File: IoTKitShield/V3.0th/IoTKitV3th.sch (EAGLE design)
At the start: 28 parts, among them J1 4P-2.0, J2 4P-2.0, J3 4P-2.0, J4 4p-2.54

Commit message: Version fuer Produktion
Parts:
- renumbered SPI(V,G,SS,MO,MI,SLK) to SPI(V,G,D9,MO,MI,SLK)
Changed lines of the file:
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@@
 <part name="A2" library="pinhead" deviceset="PINHD-2X3" device=""/>
 <part name="A0" library="pinhead" deviceset="PINHD-2X3" device=""/>
-<part name="SPI(V,G,SS,MO,MI,SLK)" library="pinhead" deviceset="PINHD-1X6" device=""/>
+<part name="SPI(V,G,D9,MO,MI,SLK)" library="pinhead" deviceset="PINHD-1X6" device=""/>
 <part name="NFC/RFID" library="pinhead" deviceset="PINHD-1X8" device=""/>
 <part name="HALL-SENSOR" library="pinhead" deviceset="PINHD-1X3" device=""/>
@@
 <attribute name="VALUE" x="146.05" y="85.09" size="1.778" layer="96"/>
 </instance>
-<instance part="SPI(V,G,SS,MO,MI,SLK)" gate="A" x="11.43" y="127" rot="R90">
+<instance part="SPI(V,G,D9,MO,MI,SLK)" gate="A" x="11.43" y="127" rot="R90">
 <attribute name="NAME" x="0.635" y="120.65" size="1.778" layer="95" rot="R90"/>
 <attribute name="VALUE" x="21.59" y="120.65" size="1.778" layer="96" rot="R90"/>
@@
 </segment>
 <segment>
-<pinref part="SPI(V,G,SS,MO,MI,SLK)" gate="A" pin="3"/>
+<pinref part="SPI(V,G,D9,MO,MI,SLK)" gate="A" pin="3"/>
 <wire x1="8.89" y1="124.46" x2="8.89" y2="114.3" width="0.1524" layer="91"/>
 <label x="8.89" y="114.3" size="1.778" layer="95" rot="R90"/>
@@
 <wire x1="11.43" y1="124.46" x2="11.43" y2="114.3" width="0.1524" layer="91"/>
 <label x="11.43" y="114.3" size="1.778" layer="95" rot="R90"/>
-<pinref part="SPI(V,G,SS,MO,MI,SLK)" gate="A" pin="4"/>
+<pinref part="SPI(V,G,D9,MO,MI,SLK)" gate="A" pin="4"/>
 <junction x="11.43" y="124.46"/>
 </segment>
@@
 </segment>
 <segment>
-<pinref part="SPI(V,G,SS,MO,MI,SLK)" gate="A" pin="5"/>
+<pinref part="SPI(V,G,D9,MO,MI,SLK)" gate="A" pin="5"/>
 <wire x1="13.97" y1="124.46" x2="13.97" y2="114.3" width="0.1524" layer="91"/>
 <label x="13.97" y="114.3" size="1.778" layer="95" rot="R90"/>
@@
 </segment>
 <segment>
-<pinref part="SPI(V,G,SS,MO,MI,SLK)" gate="A" pin="6"/>
+<pinref part="SPI(V,G,D9,MO,MI,SLK)" gate="A" pin="6"/>
 <wire x1="16.51" y1="124.46" x2="16.51" y2="114.3" width="0.1524" layer="91"/>
 <label x="16.51" y="114.3" size="1.778" layer="95" rot="R90"/>
@@
 </segment>
 <segment>
-<pinref part="SPI(V,G,SS,MO,MI,SLK)" gate="A" pin="2"/>
+<pinref part="SPI(V,G,D9,MO,MI,SLK)" gate="A" pin="2"/>
 <pinref part="SUPPLY9" gate="+5V" pin="+5V"/>
 <wire x1="6.35" y1="124.46" x2="6.35" y2="118.364" width="0.1524" layer="91"/>
@@
 </segment>
 <segment>
-<pinref part="SPI(V,G,SS,MO,MI,SLK)" gate="A" pin="1"/>
+<pinref part="SPI(V,G,D9,MO,MI,SLK)" gate="A" pin="1"/>
 <pinref part="GND6" gate="1" pin="GND"/>
 <wire x1="3.81" y1="124.46" x2="3.81" y2="116.84" width="0.1524" layer="91"/>

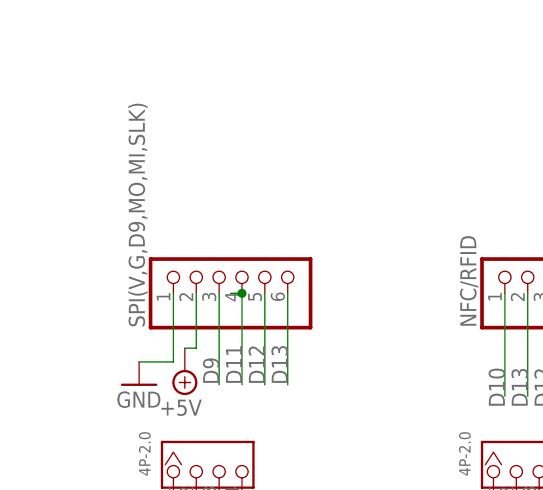
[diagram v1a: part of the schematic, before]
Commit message: Textkorrekturen
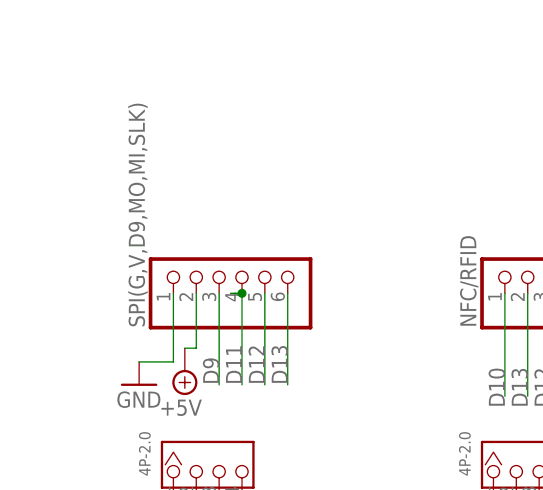
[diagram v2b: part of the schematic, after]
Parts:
- renumbered SPI(V,G,D9,MO,MI,SLK) to SPI(G,V,D9,MO,MI,SLK)
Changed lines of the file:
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@@
 <part name="A2" library="pinhead" deviceset="PINHD-2X3" device=""/>
 <part name="A0" library="pinhead" deviceset="PINHD-2X3" device=""/>
-<part name="SPI(V,G,D9,MO,MI,SLK)" library="pinhead" deviceset="PINHD-1X6" device=""/>
+<part name="SPI(G,V,D9,MO,MI,SLK)" library="pinhead" deviceset="PINHD-1X6" device=""/>
 <part name="NFC/RFID" library="pinhead" deviceset="PINHD-1X8" device=""/>
 <part name="HALL-SENSOR" library="pinhead" deviceset="PINHD-1X3" device=""/>
@@
 <attribute name="VALUE" x="146.05" y="85.09" size="1.778" layer="96"/>
 </instance>
-<instance part="SPI(V,G,D9,MO,MI,SLK)" gate="A" x="11.43" y="127" rot="R90">
+<instance part="SPI(G,V,D9,MO,MI,SLK)" gate="A" x="11.43" y="127" rot="R90">
 <attribute name="NAME" x="0.635" y="120.65" size="1.778" layer="95" rot="R90"/>
 <attribute name="VALUE" x="21.59" y="120.65" size="1.778" layer="96" rot="R90"/>
@@
 </segment>
 <segment>
-<pinref part="SPI(V,G,D9,MO,MI,SLK)" gate="A" pin="3"/>
+<pinref part="SPI(G,V,D9,MO,MI,SLK)" gate="A" pin="3"/>
 <wire x1="8.89" y1="124.46" x2="8.89" y2="114.3" width="0.1524" layer="91"/>
 <label x="8.89" y="114.3" size="1.778" layer="95" rot="R90"/>
@@
 <wire x1="11.43" y1="124.46" x2="11.43" y2="114.3" width="0.1524" layer="91"/>
 <label x="11.43" y="114.3" size="1.778" layer="95" rot="R90"/>
-<pinref part="SPI(V,G,D9,MO,MI,SLK)" gate="A" pin="4"/>
+<pinref part="SPI(G,V,D9,MO,MI,SLK)" gate="A" pin="4"/>
 <junction x="11.43" y="124.46"/>
 </segment>
@@
 </segment>
 <segment>
-<pinref part="SPI(V,G,D9,MO,MI,SLK)" gate="A" pin="5"/>
+<pinref part="SPI(G,V,D9,MO,MI,SLK)" gate="A" pin="5"/>
 <wire x1="13.97" y1="124.46" x2="13.97" y2="114.3" width="0.1524" layer="91"/>
 <label x="13.97" y="114.3" size="1.778" layer="95" rot="R90"/>
@@
 </segment>
 <segment>
-<pinref part="SPI(V,G,D9,MO,MI,SLK)" gate="A" pin="6"/>
+<pinref part="SPI(G,V,D9,MO,MI,SLK)" gate="A" pin="6"/>
 <wire x1="16.51" y1="124.46" x2="16.51" y2="114.3" width="0.1524" layer="91"/>
 <label x="16.51" y="114.3" size="1.778" layer="95" rot="R90"/>
@@
 </segment>
 <segment>
-<pinref part="SPI(V,G,D9,MO,MI,SLK)" gate="A" pin="2"/>
+<pinref part="SPI(G,V,D9,MO,MI,SLK)" gate="A" pin="2"/>
 <pinref part="SUPPLY9" gate="+5V" pin="+5V"/>
 <wire x1="6.35" y1="124.46" x2="6.35" y2="118.364" width="0.1524" layer="91"/>
@@
 </segment>
 <segment>
-<pinref part="SPI(V,G,D9,MO,MI,SLK)" gate="A" pin="1"/>
+<pinref part="SPI(G,V,D9,MO,MI,SLK)" gate="A" pin="1"/>
 <pinref part="GND6" gate="1" pin="GND"/>
 <wire x1="3.81" y1="124.46" x2="3.81" y2="116.84" width="0.1524" layer="91"/>
